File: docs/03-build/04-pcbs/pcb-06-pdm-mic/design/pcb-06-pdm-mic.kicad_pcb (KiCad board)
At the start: 2 copper layers, 12 x 14 mm, 0 parts

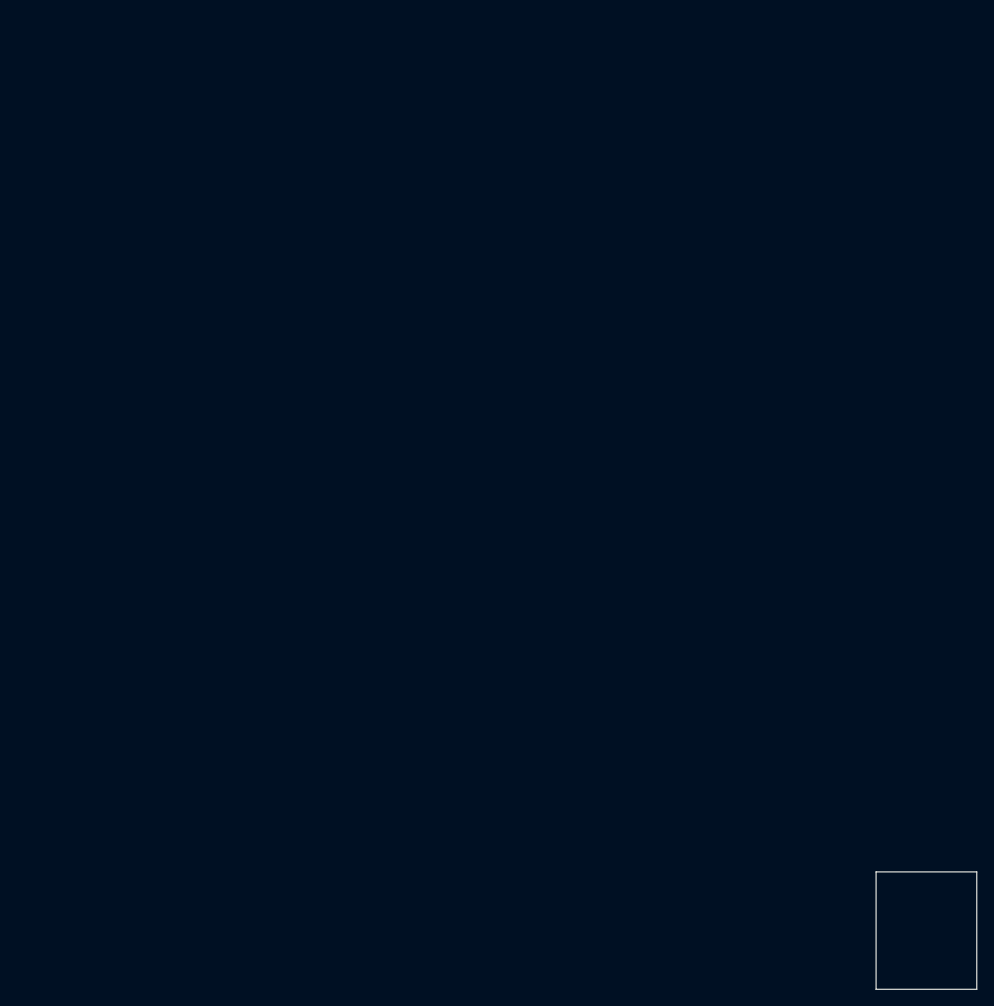
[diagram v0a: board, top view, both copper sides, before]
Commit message: build(pcbs): PCB-06 placement and routing, DRC clean (lesson 4)
- Placed by hand via KiPy: MK1 on the port (sound hole at 106,107),
  H1/H2 at +-5 mm, C2/C1 just above the mic's VDD pin, R1 beside the
  DATA pin, R2/R3 strap pair between the mic and the pads.
- W27 pads at a 2.2 mm pitch: no via fits within 3.8 mm of the port,
  so every net leaves the mic on F.Cu; a via in each pad gap lets any
  pad be fed from B.Cu without crossings.
- Routed by hand, 0.2 mm octolinear, five vias; B.Cu GND pour over the
  outer face, cut only by CLK (across the top) and +3V3 (down the pad
  column), both outside the gasket's contact ring.
- DRC with schematic parity: 0 errors, 0 unconnected; 4 cosmetic
  lib_footprint_mismatch warnings on rotated 0402s.

Co-Authored-By: Claude Opus 5.5 <noreply@anthropic.com>
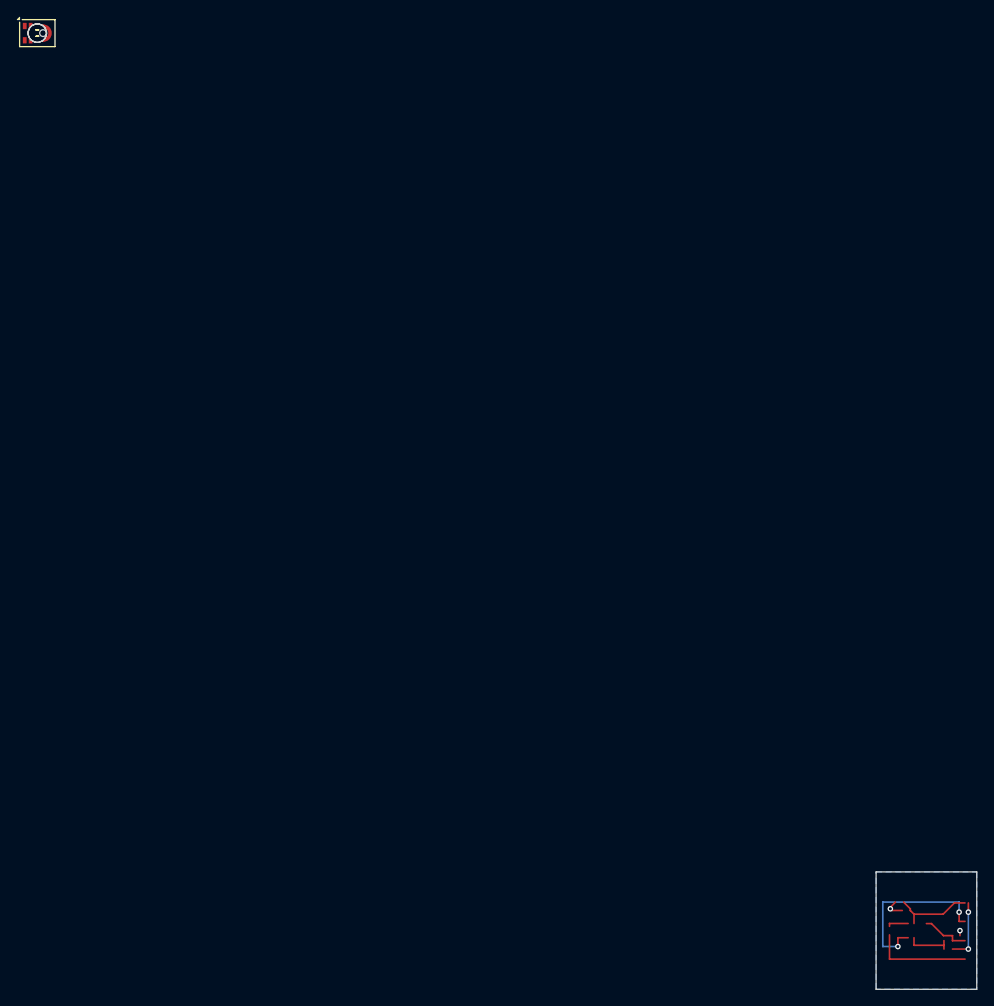
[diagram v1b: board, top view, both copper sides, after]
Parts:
- added C1: 1u X5R 10V, Capacitor_SMD:C_0402_1005Metric, F.Cu at (0.00, 0.00)
- added C2: 100n X7R 10V, Capacitor_SMD:C_0402_1005Metric, F.Cu at (0.00, 0.00)
- added H1, H2: M2 x 4 (BO-013), MountingHole:MountingHole_2.2mm_M2, F.Cu at (0.00, 0.00)
- added MK1: IM73D122V01, pcb06:IM73D122V01_PG-LLGA-5-3, F.Cu at (0.00, 0.00)
- added P1: +3V3 wire (GH pin 1), pcb06:WirePad_0.9x2.0mm, F.Cu at (0.00, 0.00)
- added P2: CLK wire (GH pin 2), pcb06:WirePad_0.9x2.0mm, F.Cu at (0.00, 0.00)
- added P3: GND wire (GH pin 3), pcb06:WirePad_0.9x2.0mm, F.Cu at (0.00, 0.00)
- added P4: DATA wire (GH pin 4), pcb06:WirePad_0.9x2.0mm, F.Cu at (0.00, 0.00)
- added R1: 100, Resistor_SMD:R_0402_1005Metric, F.Cu at (0.00, 0.00)
- added R2, R3: 1k, Resistor_SMD:R_0402_1005Metric, F.Cu at (0.00, 0.00)
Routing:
- net /CLK: track 0.00 -> 21.5 mm, vias 0 -> 2
- net +3V3: track 0.00 -> 17.1 mm, vias 0 -> 2
- net /DATA: track 0.00 -> 11.9 mm
- net GND: track 0.00 -> 8.95 mm, vias 0 -> 2
- net /LR: track 0.00 -> 5.47 mm
- net /MIC_DATA: track 0.00 -> 2.56 mm
- added copper zone on B.Cu, net GND
